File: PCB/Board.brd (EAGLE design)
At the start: 74.1 x 78.9 mm, 32 parts, among them K1 G5LE, K2 G5LE, K3 G5LE, Q1 MOSFET-NCHANNELSMD, Q2 MOSFET-NCHANNELSMD, Q3 MOSFET-NCHANNELSMD

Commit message: v2
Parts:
- removed D3, D4, D5: 1N4004, diode:DO41-10
- removed K1, K2, K3: G5LE, relay:G5LE
- removed Q2, Q3: MOSFET-NCHANNELSMD, fets:SOT23-3
- removed RAC05-K: AC/DC-CONVERTER, SousVide Library:AC/DC-CONVERTER
- removed SV2: (no value), con-lstb:MA06-1
- added C10, C5, C8: 1u, rcl:C0603
- added C11, C9: 2.2uF, rcl:C0603
- added C3, C4: 0.1u, rcl:C0603
- added C6: 10u, rcl:C0603
- added C7: 44u, rcl:C0603
- added D7: 1N4148DO35-7, diode:DO35-7
- added J1, J6: (no value), SparkFun-Connectors:1X04
- added J2, J3, J4, J5: (no value), Wurth_Elektronik_Electromechanic_Wire_to_Board_Connectors_rev19a:66100211622
- added L1: 40Ohm@100MHz, Wurth_EMC Components_WE-CBF:WE-CBF_0805(W=3.0)
- added LED1, LED2, LED3, LED4: Yellow, SparkFun-LED:LED-0603
- added OK1, OK2, OK3, OK4: MOC3031S, optocoupler:DIL6-SMD
- added OK5: 4N35, optocoupler:DIL06
- added PS1: RAC03-05SK, SousVide Library:CONV_RAC03-05SK
- added R13, R19, R23, R27: 2k, rcl:R0603
- added R14: 1k5, rcl:R0603
- added R15, R20, R28: 250, rcl:R0603
- added R16, R21, R25, R29, R36, R37: 1k, rcl:R0603
- added R17: P594, varistor:P594
- added R18, R22, R26: 500r, rcl:R0603
- added R24: 24k, rcl:R0603
- added R30: 5k, rcl:R0603
- added R31: 10k, rcl:R0603
- added R32: 100k, rcl:R0603
- added R33: 330r, rcl:R0603
- added R34, R35: 50k, rcl:R0603
- added SV1: (no value), con-lstb:MA05-1
- added T1, T2, T3, T4: (no value), transistor:SOT23-EBC
- added U$1: MDB8S, SousVide Library:4-MICRODIP
- added U$3, U$4, U$5, U$6: SST04K-800SW, SousVide Library:DPAK
- added X1: B3P-VH, con-JST VH:B3P-VH
- Q1: value MOSFET-NCHANNELSMD -> BC847SMD; device fets:SOT23-3 -> SousVide Library:SOT23
- R10: value 250 -> 500r
- R2: value 3k3 -> 10k
- R7: value 250 -> 10k
- R8: value 250 -> 1k5
- moved C1 108.0 mm to (27.4, 2.58), turned to 90 degrees
- moved JP1 105.9 mm to (53.6, 2.03), turned to 0 degrees
- moved R3 105.4 mm to (49.5, 6.35), turned to 270 degrees
- moved R4 101.2 mm to (52.3, 6.35), turned to 270 degrees
- moved THERMISTOR 99.3 mm to (43.4, 2.03), turned to 0 degrees
- moved LM117 99.3 mm to (33.5, 3.58), turned to 270 degrees
- moved R5 92.9 mm to (44.7, 6.35), turned to 90 degrees
- moved C2 92.8 mm to (36.6, 8.64), turned to 0 degrees
- moved R11 90.4 mm to (59.9, 15.2)
- moved R9 90.3 mm to (62.5, 15.2)
- moved R12 90.3 mm to (54.6, 15.2)
- moved R6 86.2 mm to (28.2, 16.5), turned to 270 degrees
- moved R2 83.7 mm to (30.5, 16.5)
- moved D2 82.3 mm to (28.2, 20.3), turned to 270 degrees
- moved STM32F070F6 80.6 mm to (41.8, 15.6)
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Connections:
- removed net GND: C1.2, C2.2, JP1.4, LM117.1, R1.2, R5.2, R6.2, RAC05-K.GND, STM32F070F6.1, STM32F070F6.15, SV2.4
- removed net N$6: D5.A, K3.2, Q2.3
- removed net RELAY1: R7.2, STM32F070F6.6
- removed net RELAY2: R8.2, STM32F070F6.9
- removed net RELAY3: R10.2, STM32F070F6.11
- removed net SWO: SV2.1
- removed net VAC(L): F1.2, K1.S, K2.S, K3.S, RAC05-K.L
- removed net VAC(L)-OUTPUT1: K1.P
- removed net VAC(L)-OUTPUT2: K3.P
- removed net VAC(L)-OUTPUT3: K2.P
- removed net VAC(N): RAC05-K.N
- new net CTRL1: R18.2, STM32F070F6.9
- new net CTRL2: R22.2, STM32F070F6.8
- new net CTRL3: R26.2, STM32F070F6.7
- new net CTRL4: R10.2, STM32F070F6.6
- new net ENCODER_A: R36.2, STM32F070F6.12, SV1.5
- new net ENCODER_B: R37.2, STM32F070F6.11, SV1.4
- new net ENCODER_BUTTON: STM32F070F6.10, SV1.3
- new net FET4: R26.1, T4.B
- new net N$10: LED1.A, R16.2
- new net N$11: J3.1, U$3.4
- new net N$12: OK2.1, R19.1
- new net N$13: OK2.4, R20.2
- new net N$14: R20.1, U$4.3
- new net N$15: LED2.A, R21.2
- new net N$16: J2.1, U$4.4
- new net N$17: LED3.C, OK3.2, T3.C
- new net N$18: OK3.1, R23.1
- new net N$20: OK3.4, R24.2
- new net N$23: R24.1, U$5.3
- new net N$24: LED3.A, R25.2
- new net N$25: J4.1, U$5.4
- new net N$26: LED4.C, OK4.2, T4.C
- new net N$27: OK4.1, R27.1
- new net N$28: OK4.4, R28.2
- new net N$29: R28.1, U$6.3
- new net N$30: LED4.A, R29.2
- new net N$31: J5.1, U$6.4
- new net N$32: D7.C, Q1.1, R30.2, U$1.4
- new net N$33: C7.1, R30.1, R33.1, U$1.3
- new net N$34: C7.2, D7.A, Q1.2
- new net N$35: OK5.2, Q1.3
- new net N$36: OK5.6, R32.1
- new net N$37: OK5.1, R33.2
- new net N$38: R34.2, U$1.1
- new net N$39: R35.2, U$1.2
- new net N$43: R2.2, STM32F070F6.1
- new net N$5: LED1.C, OK1.2, T1.C
- new net N$7: OK1.4, R15.2
- new net N$8: OK1.1, R13.1
- new net N$9: R15.1, U$3.3
- new net THERM-CALIBRATE: R14.2, R8.1, STM32F070F6.13
- new net V+: F1.2, J2.2, J3.2, J4.2, J5.2, OK1.6, OK2.6, OK3.6, OK4.6, PS1.1, R17.2, R34.1
- new net V-: PS1.4, R17.1, R35.1, U$3.1, U$4.1, U$5.1, U$6.1, X1.2
- new net ZERO-CROSS-DETECT: OK5.5, R31.2
- net +3V3: now also C10.1, C11.1, C4.1, C5.1, C9.1, J6.4, L1.1, R14.1, R31.1, R36.1, R37.1, R7.1, SV1.2; no longer R2.2, STM32F070F6.5, SV2.6
- net +5V: now also C6.1, PS1.3, R13.2, R16.1, R19.2, R21.1, R23.2, R25.1, R27.2, R29.1; no longer D3.C, D4.C, D5.C, K1.1, K2.1, K3.1, RAC05-K.+5V
- net FET1: now also R18.1, T2.B; no longer Q1.1, R7.1
- net FET2: now also R22.1, T3.B; no longer Q2.1, R8.1
- net FET3: now also T1.B; no longer Q3.1
- net N$19: now also J1.4; no longer SV2.5
- net N$21: now also J1.2; no longer SV2.3
- net N$22: now also J1.1; no longer SV2.2
- net N$3: now also C3.1, C8.1, L1.2, STM32F070F6.5; no longer D4.A, K1.2, Q1.3
- net N$4: now also LED2.C, OK2.2, T2.C; no longer D3.A, K2.2, Q3.3
- net NRST: now also R7.2; no longer R2.1
- net PE: now also C1.2, C10.2, C11.2, C2.2, C3.2, C4.2, C5.2, C6.2, C8.2, C9.2, J1.3, J6.3, JP1.4, LM117.1, OK5.4, PS1.2, R1.2, R2.1, R32.2, R5.2, R6.2, R8.2, STM32F070F6.15, SV1.1, T1.E, T2.E, T3.E, T4.E, X1.1; no longer Q1.2, Q2.2, Q3.2
- net RX: now also J6.2
- net TX: now also J6.1
- net VAC(L)-INPUT: now also X1.3
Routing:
- net V+: track 0.00 -> 205.4 mm, vias 0 -> 3
- net GND: track 154.6 -> 0.00 mm, vias 4 -> 0
- net VAC(L): track 141.1 -> 0.00 mm, vias 1 -> 0
- net V-: track 0.00 -> 127.9 mm, vias 0 -> 4
- net VAC(N): track 90.0 -> 0.00 mm, vias 4 -> 0
- net +5V: track 222.1 -> 135.6 mm, vias 1 -> 5
- net VAC(L)-OUTPUT3: track 62.7 -> 0.00 mm, vias 1 -> 0
- net PE: track 2.71 -> 61.3 mm, vias 0 -> 10
- net N$6: track 52.6 -> 0.00 mm
- net +3V3: track 80.3 -> 129.2 mm, vias 1 -> 5
- net CTRL4: track 0.00 -> 42.5 mm, vias 0 -> 2
- net ENCODER_BUTTON: track 0.00 -> 39.7 mm, vias 0 -> 2
- net ENCODER_A: track 0.00 -> 37.1 mm, vias 0 -> 3
- net CTRL3: track 0.00 -> 36.0 mm, vias 0 -> 2
- net ENCODER_B: track 0.00 -> 35.2 mm, vias 0 -> 2
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- added copper zone on layer 16, net PE
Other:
- board size 74.1 x 78.9 mm -> 73.9 x 62.2 mm
- board text added: "SousVide rev 3 by M.Yablonovitch JUL 2020"
- board text removed: "3.3v"
- board text removed: "3v3"
- board text removed: "5v"
- board text removed: "L"
- board text removed: "L-INPUT"
- board text removed: "N"
- board text removed: "RX"
- board text removed: "SousVide rev.3 Design By: M.Yablonovitch AUG 2019"
- board text removed: "TX"

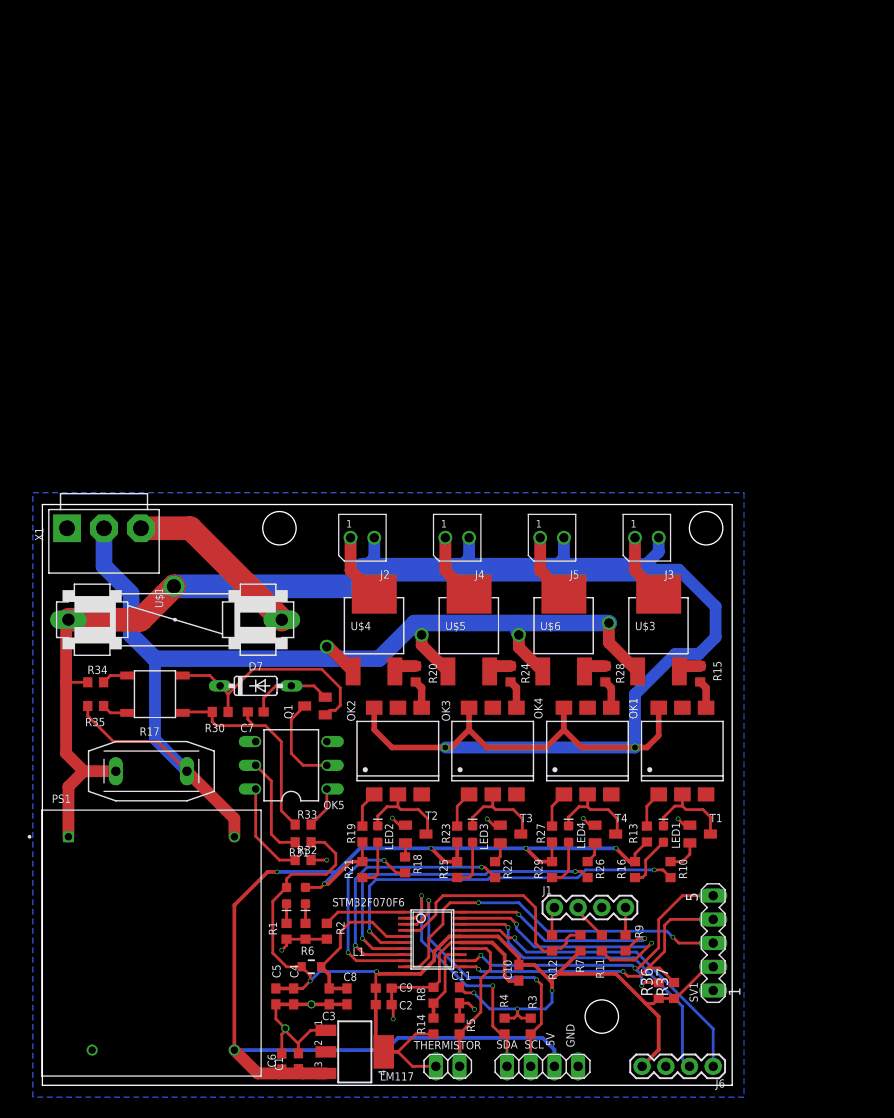
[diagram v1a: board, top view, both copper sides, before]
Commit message: started v4 redesign
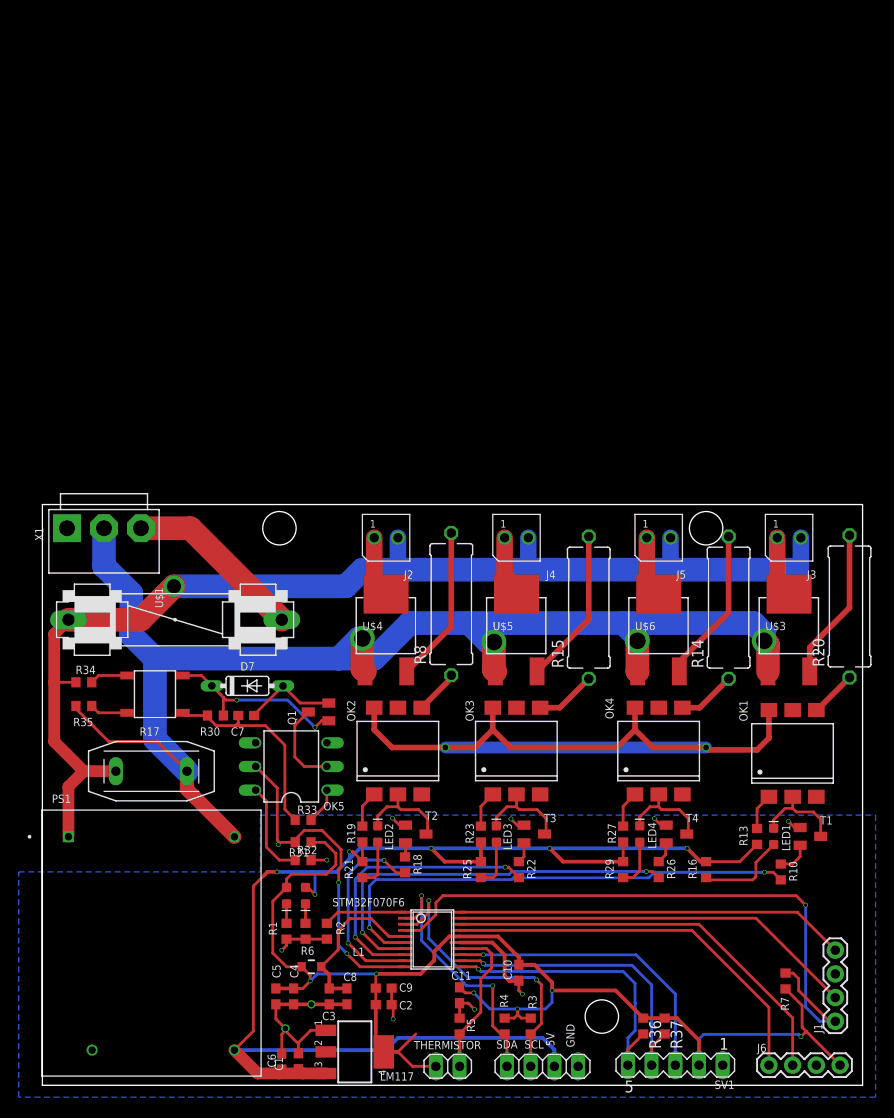
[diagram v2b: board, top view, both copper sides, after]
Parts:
- removed R11, R12, R28, R9: 250, rcl:R0603
- removed R24: 24k, rcl:R0603
- R14, R8: value 1k5 -> (none); device rcl:R0603 -> rcl:P0613/15
- R15, R20: value 250 -> (none); device rcl:R0603 -> rcl:P0613/15
- moved R14 54.9 mm to (73.5, 51.2)
- moved R20 47.0 mm to (86.5, 51.3), turned to 90 degrees
- moved R8 42.0 mm to (43.8, 51.6)
- moved J1 32.5 mm to (85.0, 6.86), turned to 90 degrees
- moved R7 22.3 mm to (79.6, 11.2)
- moved J3 15.2 mm to (80.0, 58.7)
- moved U$3 14.0 mm to (80.0, 49.3)
- moved R15 13.9 mm to (58.5, 51.2), turned to 90 degrees
- moved SV1 13.7 mm to (67.8, 2.16), turned to 180 degrees
- moved OK1 11.8 mm to (80.4, 35.6)
- moved R13 11.8 mm to (76.6, 26.7)
- moved T1 11.8 mm to (82.3, 26.7)
- moved LED1 11.8 mm to (78.4, 26.7)
- moved R10 11.8 mm to (79.1, 22.9)
- moved J5 11.4 mm to (66.0, 58.7)
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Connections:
- removed net N$19: J1.4, R9.2
- removed net N$21: J1.2, R11.2
- removed net N$22: J1.1, R12.2
- removed net THERM-CALIBRATE: R14.2, R8.1, STM32F070F6.13
- net +3V3: no longer R14.1
- net ENCODER_A: now also STM32F070F6.11; no longer STM32F070F6.12
- net ENCODER_B: now also STM32F070F6.12; no longer STM32F070F6.11
- net ENCODER_BUTTON: now also STM32F070F6.13; no longer STM32F070F6.10
- net N$13: now also R8.1; no longer R20.2
- net N$14: now also R8.2; no longer R20.1
- net N$20: now also R15.1; no longer R24.2
- net N$23: now also R15.2; no longer R24.1
- net N$28: now also R14.1; no longer R28.2
- net N$29: now also R14.2; no longer R28.1
- net N$7: now also R20.1; no longer R15.2
- net N$9: now also R20.2; no longer R15.1
- net NRST: now also J1.1; no longer R12.1
- net PE: no longer R8.2
- net SWCLK: now also J1.4; no longer R9.1
- net SWDIO: now also J1.2; no longer R11.1
- net ZERO-CROSS-DETECT: now also STM32F070F6.10
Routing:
- net NRST: track 26.7 -> 68.6 mm, vias 0 -> 1
- net ZERO-CROSS-DETECT: track 11.0 -> 36.1 mm, vias 0 -> 3
- net V-: track 127.9 -> 149.4 mm
- net SWCLK: track 23.8 -> 41.9 mm, vias 2 -> 0
- net +5V: track 135.6 -> 151.6 mm, vias 5 -> 6
- net SWDIO: track 28.8 -> 43.8 mm, vias 2 -> 0
- net N$14: track 2.47 -> 16.8 mm
- net N$23: track 2.47 -> 16.7 mm
- net N$29: track 2.47 -> 16.6 mm
- net N$9: track 2.47 -> 16.3 mm
- net CTRL4: track 42.5 -> 53.9 mm
- net +3V3: track 129.2 -> 140.7 mm, vias 5 -> 6
- net RX: track 35.2 -> 44.9 mm, vias 1 -> 0
- net THERM-CALIBRATE: track 8.72 -> 0.00 mm
- net PE: track 61.3 -> 52.9 mm, vias 10 -> 11
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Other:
- board size 73.9 x 62.2 mm -> 87.9 x 62.2 mm
